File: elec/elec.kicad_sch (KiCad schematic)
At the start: 73 parts, among them J1 USB_C_Receptacle, J2 Conn_01x05, J3 Screw_Terminal_01x02, J4 Conn_01x03, J5 Conn_01x03, Q1 AO3401A, SW2 SW_Push, SW3 SW_Push, SW4 SW_Push, SW5 SW_Push, SW6 SW_Push, SW7 SW_Push, U1 HUSB238A-xxxxx-QN16R, U2 SY8303AIC, U3 STM32G030K8T6, U4 TPS55289RYQR

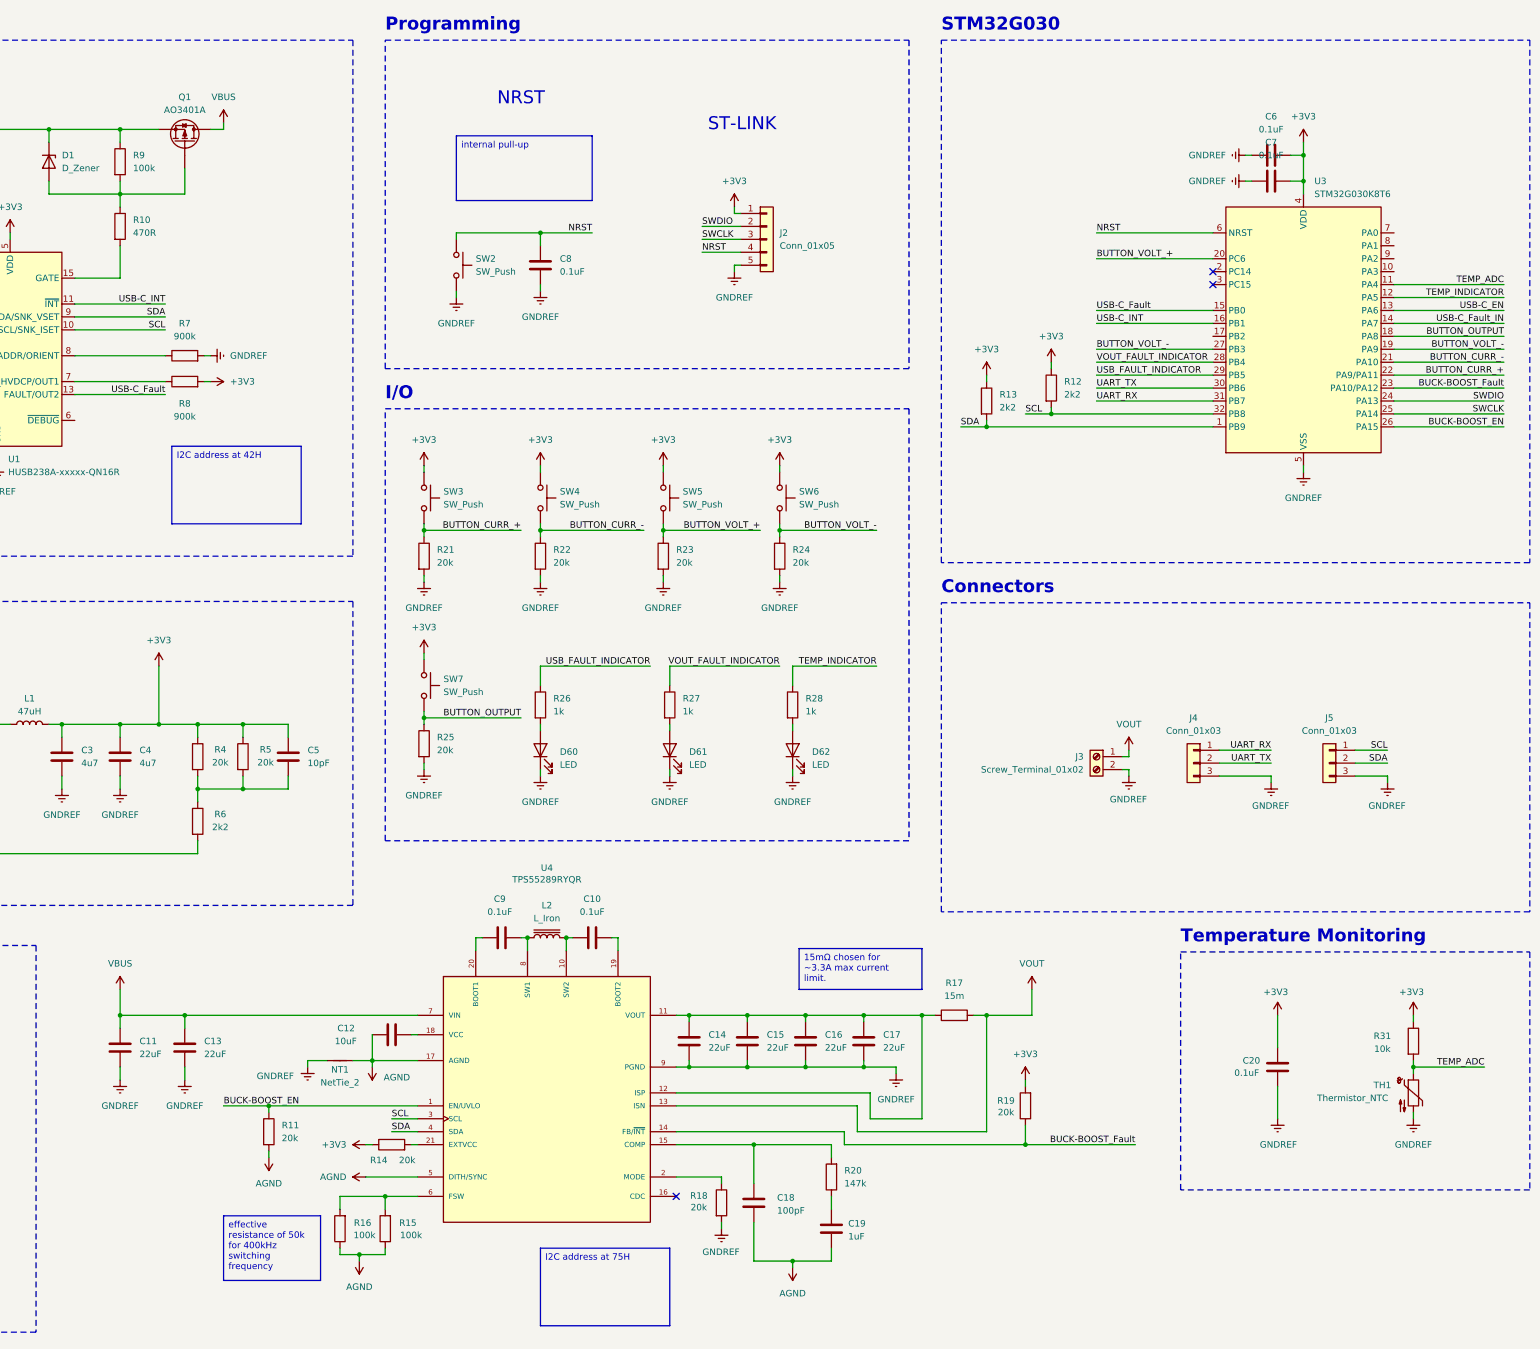
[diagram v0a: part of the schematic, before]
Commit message: Populate LCSC Params, Assign Footprints, Update STM32CubeMX
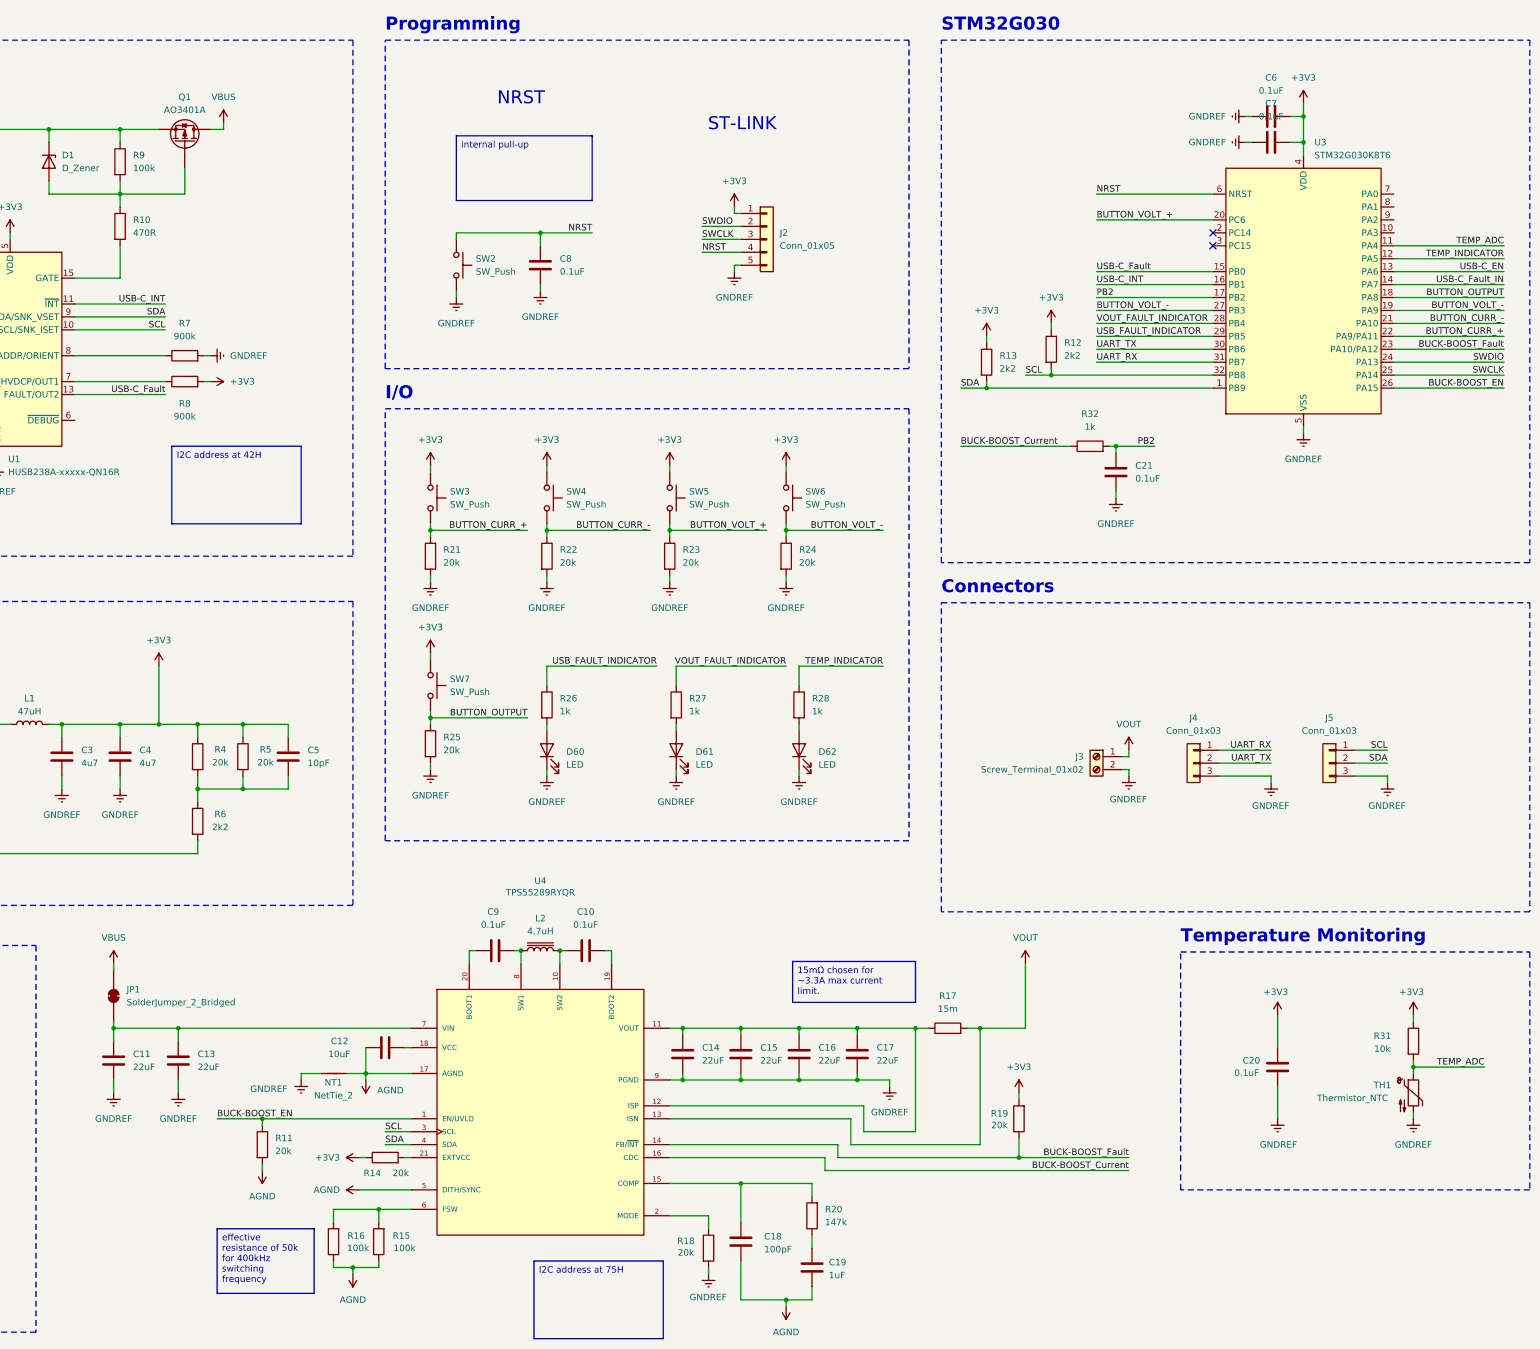
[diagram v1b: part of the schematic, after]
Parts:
- added C21: 0.1uF, Capacitor_SMD:C_0603_1608Metric, symbol Device:C
- added JP1: SolderJumper_2_Bridged, Jumper:SolderJumper-2_P1.3mm_Bridged2Bar_RoundedPad1.0x1.5mm, symbol Jumper:SolderJumper_2_Bridged
- added R32: 1k, Resistor_SMD:R_0603_1608Metric, symbol Device:R
- C1, C11, C12, C13, C14, C15, C16, C17, C3, C4: footprint (none) -> Capacitor_SMD:C_1206_3216Metric
- C10, C18, C19, C2, C20, C5, C6, C7, C8, C9: footprint (none) -> Capacitor_SMD:C_0603_1608Metric
- D1: footprint (none) -> Diode_SMD:D_SOD-123
- D60, D61, D62: footprint (none) -> LED_SMD:LED_0603_1608Metric
- J1: footprint (none) -> Connector_USB:USB_C_Receptacle_GCT_USB4105-xx-A_16P_TopMnt_Horizontal
- J2: footprint (none) -> Connector_PinHeader_2.54mm:PinHeader_1x05_P2.54mm_Vertical
- J3: footprint (none) -> TerminalBlock_MetzConnect:TerminalBlock_MetzConnect_360271_1x01_Horizontal_ScrewM3.0_Boxed
- J4, J5: footprint (none) -> Connector_PinHeader_2.54mm:PinHeader_1x03_P2.54mm_Vertical
- L1: footprint (none) -> Inductor_SMD:L_12x12mm_H8mm; LCSC (none) -> C9906
- L2: value L_Iron -> 4.7uH; footprint (none) -> Inductor_SMD:L_12x12mm_H8mm; LCSC (none) -> C24548
- NT1: footprint (none) -> NetTie:NetTie-2_SMD_Pad2.0mm
- R1, R10, R11, R12, R13, R14, R15, R16, R18, R19, R2, R20, R21, R22, R23, R24, R25, R26, R27, R28, R3, R31, R4, R5, R6, R7, R8, R9, TH1: footprint (none) -> Resistor_SMD:R_0603_1608Metric
- R17: footprint (none) -> Resistor_SMD:R_2512_6332Metric; LCSC (none) -> C459682
- SW2, SW3, SW4, SW5, SW6, SW7: footprint (none) -> Button_Switch_THT:SW_Tactile_SPST_Angled_PTS645Vx58-2LFS; LCSC (none) -> C86476
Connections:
- net GNDREF: now also C21.1
- net VBUS: now also JP1.2 (B); no longer C11.1, C13.1, U4.7 (VIN)
- net BUCK-BOOST_Current: now reaches U4.16 (CDC)
- net BUCK-BOOST_Current: now also R32.1
- net PB2: now reaches U3.17 (PB2)
- net PB2: now also C21.2, R32.2
- new net: C11.1, C13.1, JP1.1 (A), U4.7 (VIN)
- no-connect marks 11 -> 10
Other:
- moved on the sheet: C10, C11, C12, C13, C14, C15, C16, C17, C18, C19, C6, C7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

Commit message: Start PCB Layout Draft
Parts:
- L1: footprint Inductor_SMD:L_12x12mm_H8mm -> Inductor_SMD:L_APV_ANR5040; LCSC C9906 -> C9392
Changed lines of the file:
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@@
 			)
 		)
-		(property "Footprint" "Inductor_SMD:L_12x12mm_H8mm"
+		(property "Footprint" "Inductor_SMD:L_APV_ANR5040"
 			(at 107.95 157.48 0)
 			(hide yes)
@@
 			)
 		)
-		(property "Datasheet" "https://www.lcsc.com/datasheet/C9906.pdf?spm=wm.sxq.inf.ggs&lcsc_vid=TldfUgIFRgcMXgYERlcMUAVSFVgIVAdUT1ZbUFNSRFcxVlNeRlVcUlBRRllXVTsOAxUeFF5JWBYZEEoKFBINSQcJGk4dAgUUFAk%3D"
+		(property "Datasheet" "https://www.lcsc.com/datasheet/C9392.pdf?spm=wm.sxq.inf.ggs&lcsc_vid=TldfUgIFRgcMXgYERlcMUAVSFVgIVAdUT1ZbUFNSRFcxVlNeRlRdVFRfQVVcXzsOAxUeFF5JWBYZEEoKFBINSQcJGk4%3D"
 			(at 107.95 157.48 0)
 			(hide yes)
@@
 			)
 		)
-		(property "LCSC" "C9906"
+		(property "LCSC" " C9392"
 			(at 107.95 157.48 90)
 			(hide yes)

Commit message: Layout of everything except display
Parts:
- added H1: MountingHole_Pad, MountingHole:MountingHole_2.2mm_M2_Pad_Via, symbol Mechanical:MountingHole_Pad
- added H2, H3, H4: MountingHole, MountingHole:MountingHole_2.2mm_M2_Pad_Via, symbol Mechanical:MountingHole
- added R33: 0R, Resistor_SMD:R_0603_1608Metric, symbol Device:R
- J3: footprint TerminalBlock_MetzConnect:TerminalBlock_MetzConnect_360271_1x01_Horizontal_ScrewM3.0_Boxed -> TerminalBlock_CUI:TerminalBlock_CUI_TB007-508-02_1x02_P5.08mm_Horizontal
- SW2: footprint Button_Switch_THT:SW_Tactile_SPST_Angled_PTS645Vx58-2LFS -> usbc-psu-footprints:SKRKAEE020; LCSC C86476 -> C115357
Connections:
- net GNDREF: now also R33.2
- new net CHASSIS_GND: H1.1, R33.1
- no-connect marks 10 -> 14
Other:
- note added: "Mounting Holes"

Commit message: PCB layout
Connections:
- net CV_INDICATOR: now reaches U3.7 (PA0)
- net CC_INDICATOR: now reaches U3.8 (PA1)
- net OCP_INDICATOR: now reaches U3.9 (PA2)
- no-connect marks 14 -> 11
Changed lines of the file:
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@@
 	)
 	(no_connect
-		(at 375.92 53.34)
-	)
-	(no_connect
 		(at 58.42 83.82)
 	)
 	(no_connect
-		(at 375.92 58.42)
-	)
-	(no_connect
 		(at 58.42 99.06)
 	)
@@
 	)
 	(no_connect
-		(at 375.92 55.88)
-	)
-	(no_connect
 		(at 340.36 63.5)
 	)
@@
 	(wire
 		(pts
+			(xy 375.92 55.88) (xy 397.51 55.88)
+		)
+		(stroke
+			(width 0)
+			(type default)
+		)
+	)
+	(wire
+		(pts
 			(xy 124.46 227.33) (xy 124.46 229.87)
 		)
@@
 	(wire
 		(pts
+			(xy 375.92 58.42) (xy 397.51 58.42)
+		)
+		(stroke
+			(width 0)
+			(type default)
+		)
+	)
+	(wire
+		(pts
 			(xy 101.6 106.68) (xy 101.6 105.41)
 		)
@@
 	(wire
 		(pts
+			(xy 375.92 53.34) (xy 397.51 53.34)
+		)
+		(stroke
+			(width 0)
+			(type default)
+		)
+	)
+	(wire
+		(pts
 			(xy 375.92 66.04) (xy 397.51 66.04)
 		)
@@
 		)
 	)
+	(label "OCP_INDICATOR"
+		(at 397.51 58.42 180)
+		(effects
+			(font
+				(size 1.27 1.27)
+			)
+			(justify right bottom)
+		)
+	)
 	(label "SDA"
 		(at 134.62 77.47 180)
@@
 		)
 	)
+	(label "CV_INDICATOR"
+		(at 397.51 53.34 180)
+		(effects
+			(font
+				(size 1.27 1.27)
+			)
+			(justify right bottom)
+		)
+	)
 	(label "SCL"
 		(at 99.06 236.22 180)
@@
 		(effects
 			(font
+				(size 1.27 1.27)
+			)
+			(justify right bottom)
+		)
+	)
+	(label "CC_INDICATOR"
+		(at 397.51 55.88 180)
+		(effects
+			(font

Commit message: Completed Routing
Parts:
- D1: LCSC (none) -> C2103
- Q1: value AO3401A -> AO4419; footprint Package_TO_SOT_SMD:SOT-23 -> Package_SO:SOIC-8-1EP_3.9x4.9mm_P1.27mm_EP2.29x3mm_ThermalVias; LCSC C15127 -> C29205
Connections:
- net BUTTON_CURR_+: now also U3.20 (PC6); no longer U3.22 (PA9/PA11)
- net BUTTON_OUTPUT: now also U3.22 (PA9/PA11); no longer U3.18 (PA8)
- net BUTTON_VOLT_+: now also U3.18 (PA8); no longer U3.20 (PC6)
- net BUTTON_VOLT_-: no longer U3.27 (PB3)
- net CV_INDICATOR: now also U3.9 (PA2); no longer U3.7 (PA0)
- net OCP_INDICATOR: now also U3.7 (PA0); no longer U3.9 (PA2)
- net TEMP_INDICATOR: now also U3.29 (PB5); no longer U3.12 (PA5)
- net USB_FAULT_INDICATOR: now also U3.12 (PA5); no longer U3.29 (PB5)
- no-connect marks 11 -> 13
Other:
- sheet display ports: added CC_INDICATOR, CV_INDICATOR, OCP_INDICATOR; removed none

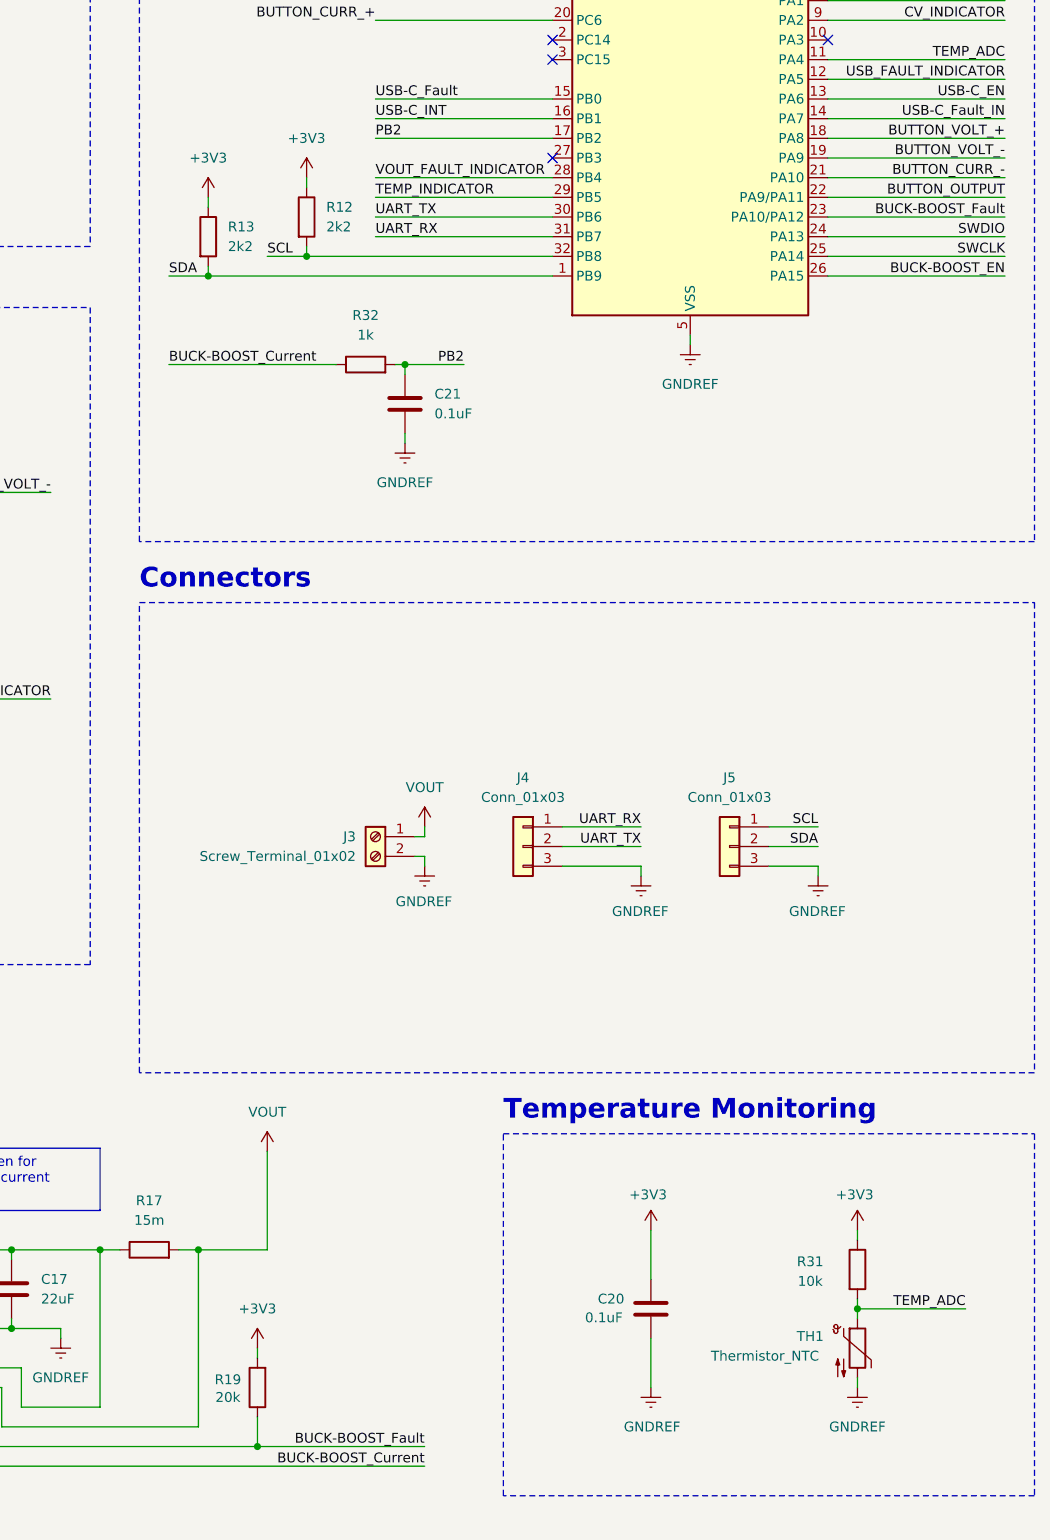
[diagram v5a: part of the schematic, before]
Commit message: Added Bleed Resistor, Added Buzzer
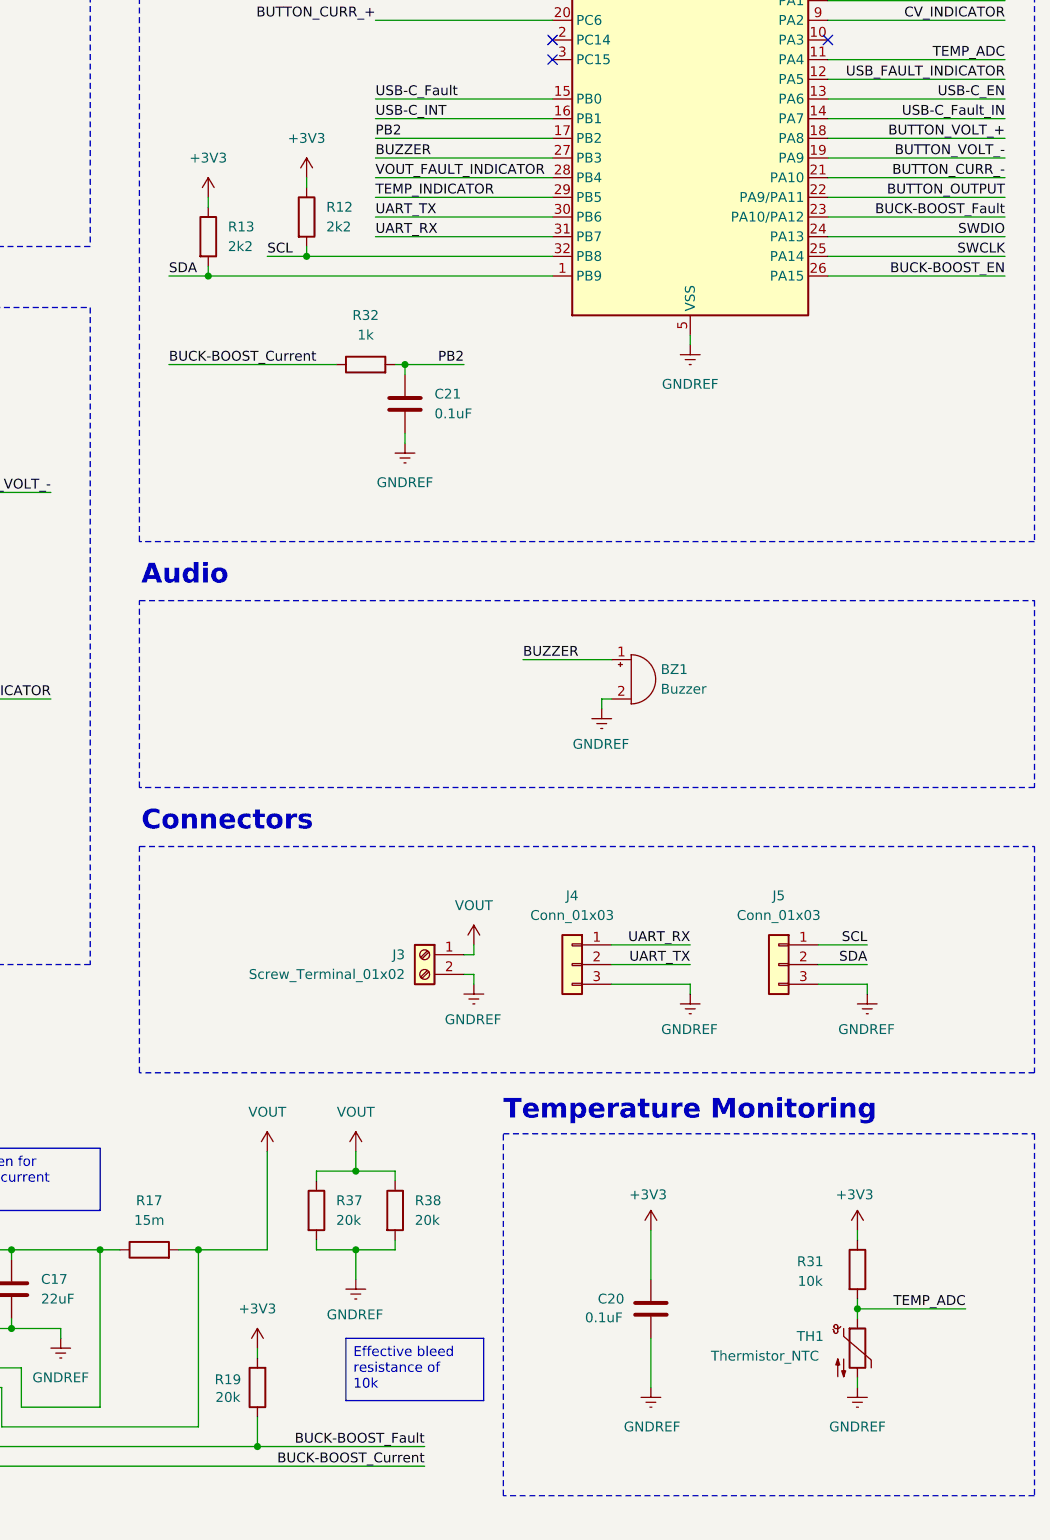
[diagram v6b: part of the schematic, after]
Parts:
- added BZ1: Buzzer, Buzzer_Beeper:Buzzer_Murata_PKMCS0909E, symbol Device:Buzzer
- added R37, R38: 20k, Resistor_SMD:R_0603_1608Metric, symbol Device:R
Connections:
- net GNDREF: now also BZ1.2 (-), R37.2, R38.2
- net VOUT: now also R37.1, R38.1
- net BUZZER: now reaches U3.27 (PB3)
- net BUZZER: now also BZ1.1 (+)
- no-connect marks 13 -> 12
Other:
- note added: "Audio"
- moved on the sheet: J3, J4, J5
